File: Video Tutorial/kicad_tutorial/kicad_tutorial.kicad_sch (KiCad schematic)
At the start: 50 parts, among them J1 Screw_Terminal_01x02, J2 SWD, J3 Conn_01x04, J4 Conn_01x04, J5 USB_B_Micro, Q1 AO3401A, SW1 SW_SPDT, U1 MP2359DJ-LF-Z, U2 STM32F405RGT6, U3 USBLC6-2SC6, Y1 16MHz

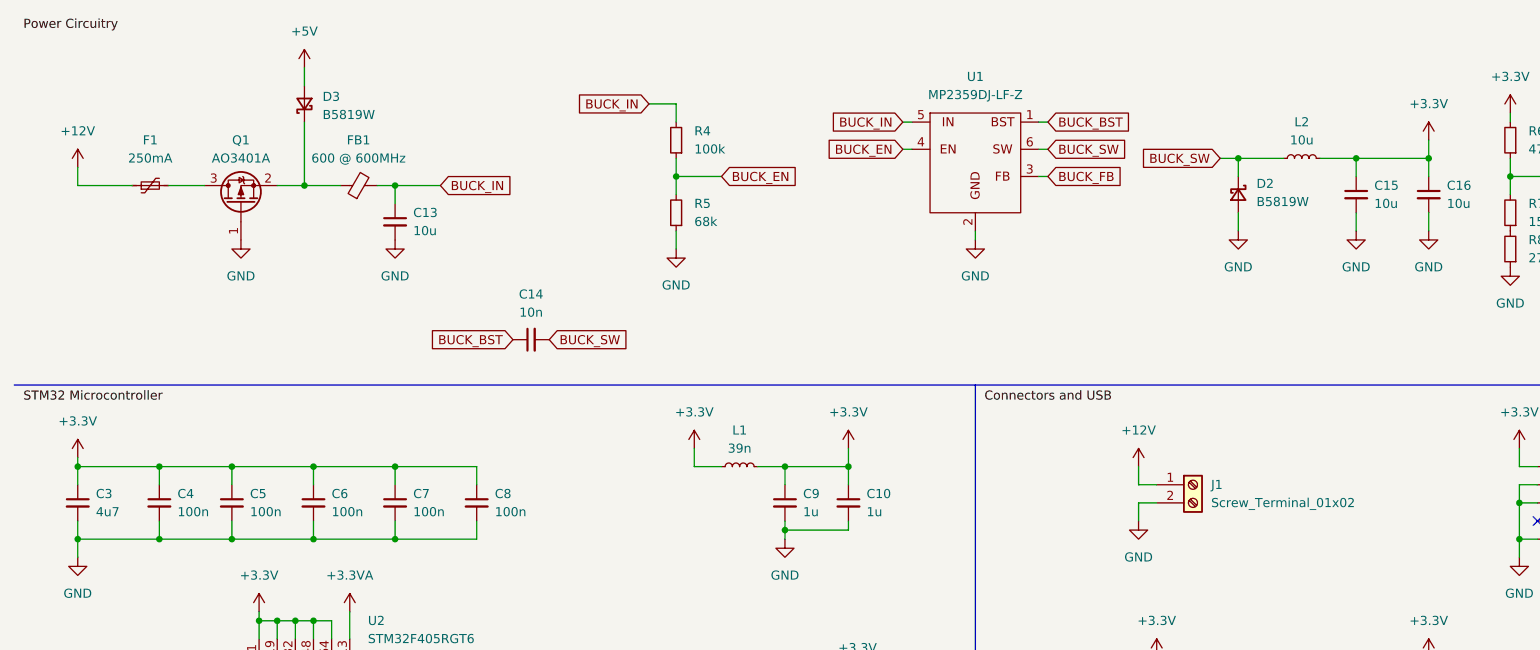
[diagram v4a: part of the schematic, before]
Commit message: Added notes for Chapter: Improving the layout, finer details
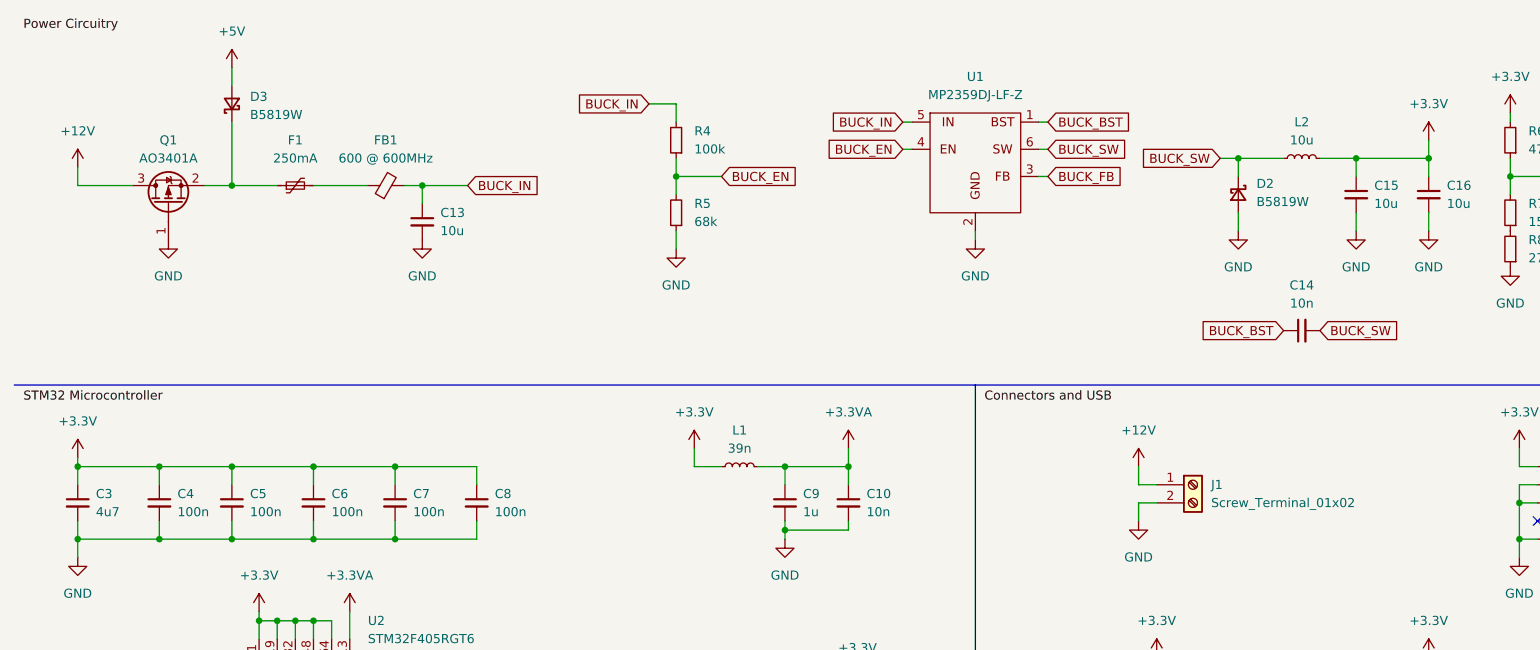
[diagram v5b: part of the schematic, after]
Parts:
- C10: value 1u -> 10n
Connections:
- net +12V: now also Q1.3 (D); no longer F1.1
- net +3.3V: no longer C10.1, C9.1, L1.2
- net +3.3VA: now also C10.1, C9.1, L1.2
- net at D3.1 (K), Q1.2 (S): now also F1.1; no longer FB1.1
- net at F1.2: now also FB1.1; no longer Q1.3 (D)
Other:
- moved on the sheet: C13, C14, D3, F1, FB1, Q1

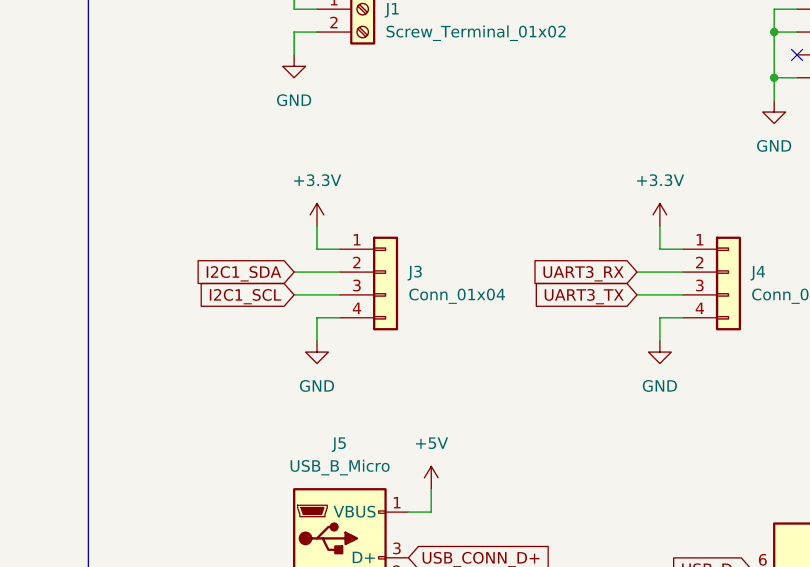
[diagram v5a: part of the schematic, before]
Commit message: Added notes for Chapter: Design rules checker (DRC)
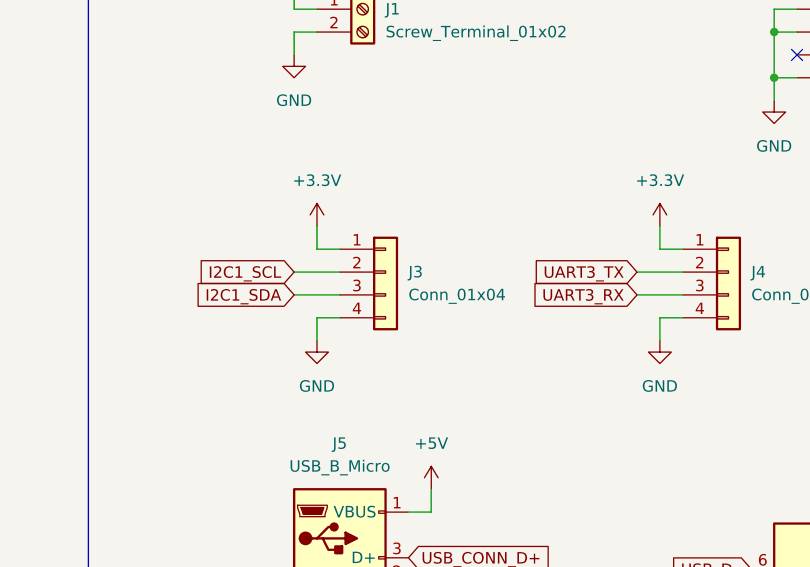
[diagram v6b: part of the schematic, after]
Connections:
- net I2C1_SCL: now also J3.2 (Pin_2); no longer J3.3 (Pin_3)
- net I2C1_SDA: now also J3.3 (Pin_3); no longer J3.2 (Pin_2)
- net UART3_RX: now also J4.3 (Pin_3); no longer J4.2 (Pin_2)
- net UART3_TX: now also J4.2 (Pin_2); no longer J4.3 (Pin_3)
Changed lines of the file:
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@@
     )
   )
-  (global_label "UART3_RX" (shape input) (at 207.01 107.95 180) (fields_autoplaced)
+  (global_label "UART3_RX" (shape input) (at 207.01 110.49 180) (fields_autoplaced)
     (effects (font (size 1.27 1.27)) (justify right))
-    (property "Intersheetrefs" "${INTERSHEET_REFS}" (at 194.7909 107.95 0)
+    (property "Intersheetrefs" "${INTERSHEET_REFS}" (at 194.7909 110.49 0)
       (effects (font (size 1.27 1.27)) (justify right) hide)
     )
@@
     )
   )
-  (global_label "I2C1_SCL" (shape input) (at 168.91 110.49 180) (fields_autoplaced)
+  (global_label "I2C1_SCL" (shape input) (at 168.91 107.95 180) (fields_autoplaced)
     (effects (font (size 1.27 1.27)) (justify right))
-    (property "Intersheetrefs" "${INTERSHEET_REFS}" (at 157.2352 110.49 0)
+    (property "Intersheetrefs" "${INTERSHEET_REFS}" (at 157.2352 107.95 0)
       (effects (font (size 1.27 1.27)) (justify right) hide)
     )
@@
     )
   )
-  (global_label "I2C1_SDA" (shape input) (at 168.91 107.95 180) (fields_autoplaced)
+  (global_label "I2C1_SDA" (shape input) (at 168.91 110.49 180) (fields_autoplaced)
     (effects (font (size 1.27 1.27)) (justify right))
-    (property "Intersheetrefs" "${INTERSHEET_REFS}" (at 157.1747 107.95 0)
+    (property "Intersheetrefs" "${INTERSHEET_REFS}" (at 157.1747 110.49 0)
       (effects (font (size 1.27 1.27)) (justify right) hide)
     )
@@
     )
   )
-  (global_label "UART3_TX" (shape input) (at 207.01 110.49 180) (fields_autoplaced)
+  (global_label "UART3_TX" (shape input) (at 207.01 107.95 180) (fields_autoplaced)
     (effects (font (size 1.27 1.27)) (justify right))
-    (property "Intersheetrefs" "${INTERSHEET_REFS}" (at 195.0933 110.49 0)
+    (property "Intersheetrefs" "${INTERSHEET_REFS}" (at 195.0933 107.95 0)
       (effects (font (size 1.27 1.27)) (justify right) hide)
     )

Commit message: Completed KiCad Tutorial Video
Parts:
- C1, C2: LCSC Part # (none) -> C23630
- C10, C14: LCSC Part # (none) -> C15195
- C11, C12: LCSC Part # (none) -> C1547
- C13, C15, C16: LCSC Part # (none) -> C13585
- C3: LCSC Part # (none) -> C19666
- C4, C5, C6, C7, C8: LCSC Part # (none) -> C1525
- C9: LCSC Part # (none) -> C52923
- D1: LCSC Part # (none) -> C72041
- D2, D3: LCSC Part # (none) -> C8598
- D4: LCSC Part # (none) -> C2286
- F1: LCSC Part # (none) -> C369159
- L1: LCSC Part # (none) -> C26443
- L2: LCSC Part # (none) -> C139506
- Q1: LCSC Part # (none) -> C15127
- R1: LCSC Part # (none) -> C25744
- R10, R9: LCSC Part # (none) -> C25879
- R11: LCSC Part # (none) -> C21190
- R2: LCSC Part # (none) -> C25118
- R3: LCSC Part # (none) -> C22843
- R4: LCSC Part # (none) -> C25803
- R5: LCSC Part # (none) -> C23231
- R6: LCSC Part # (none) -> C25819
- R7: LCSC Part # (none) -> C22809
- R8: LCSC Part # (none) -> C22966
- U1: LCSC Part # (none) -> C14259
- U2: LCSC Part # (none) -> C15742
- U3: LCSC Part # (none) -> C7519
- Y1: LCSC Part # (none) -> C13738
